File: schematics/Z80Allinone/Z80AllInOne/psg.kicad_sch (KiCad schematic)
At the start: 19 parts, among them J5 Conn_01x03_Male, J7 KEYBOARD_HEADER, U20 74LS02, U21 AY-3-8910, U22 LM386

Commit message: Latest modifications of All-in-one PCB
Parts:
- removed J5: Conn_01x03_Male, Connector_PinHeader_2.54mm:PinHeader_1x03_P2.54mm_Vertical, symbol Connector:Conn_01x03_Male
- removed JP4: PREAMP_MONO, Connector_PinHeader_2.54mm:PinHeader_2x03_P2.54mm_Vertical, symbol Connector_Generic:Conn_02x03_Odd_Even
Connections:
- net at R12.2, R13.2: now also U21.3 (ACH_B), U21.38 (ACH_C), U21.4 (ACH_A)
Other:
- moved on the sheet: C30, C31, C32, C33, C42, C43, R12, R13, R14, R15, SPEAKER1, U22

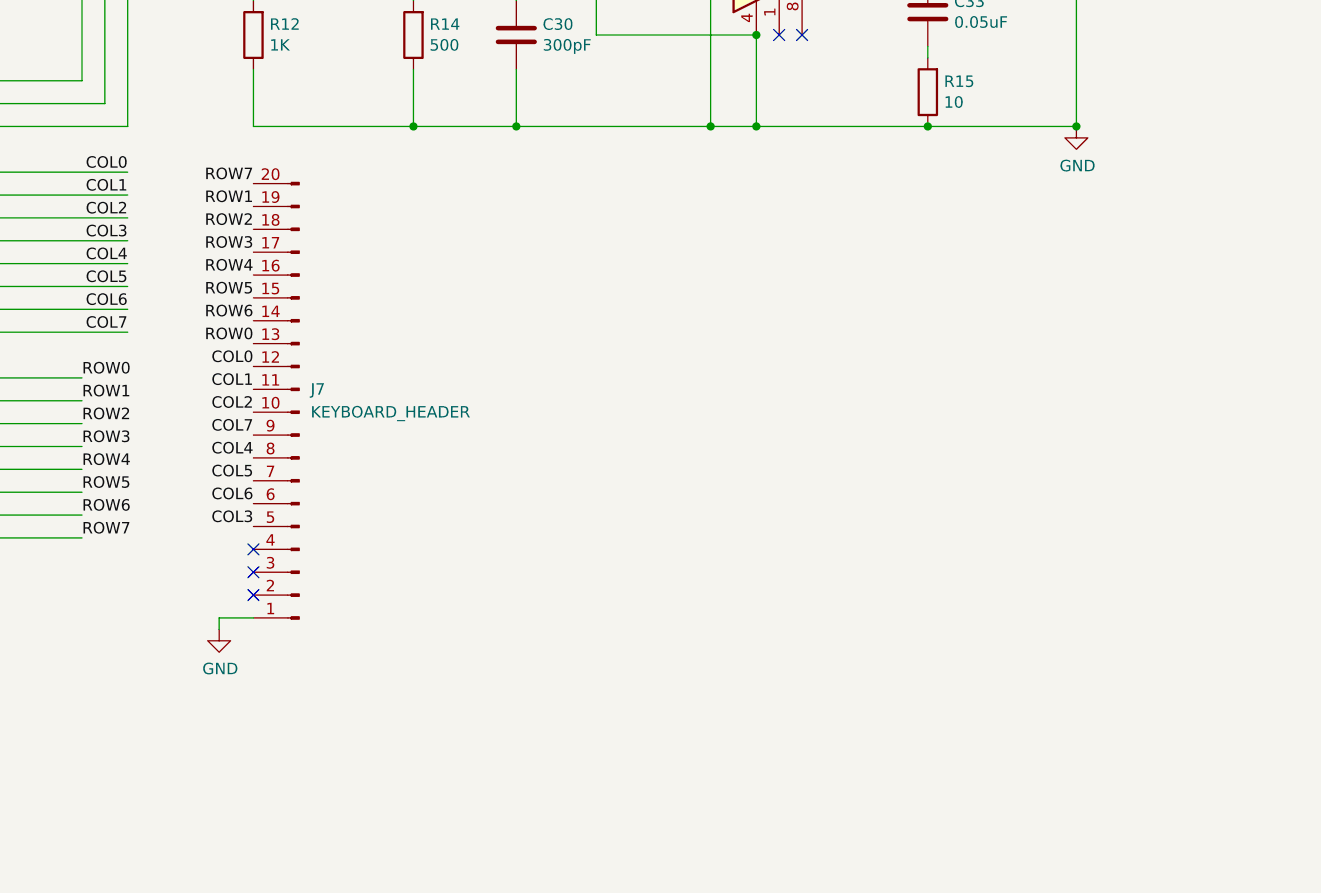
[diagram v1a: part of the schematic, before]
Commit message: Latest changes and replace CTC for 8253 PIT
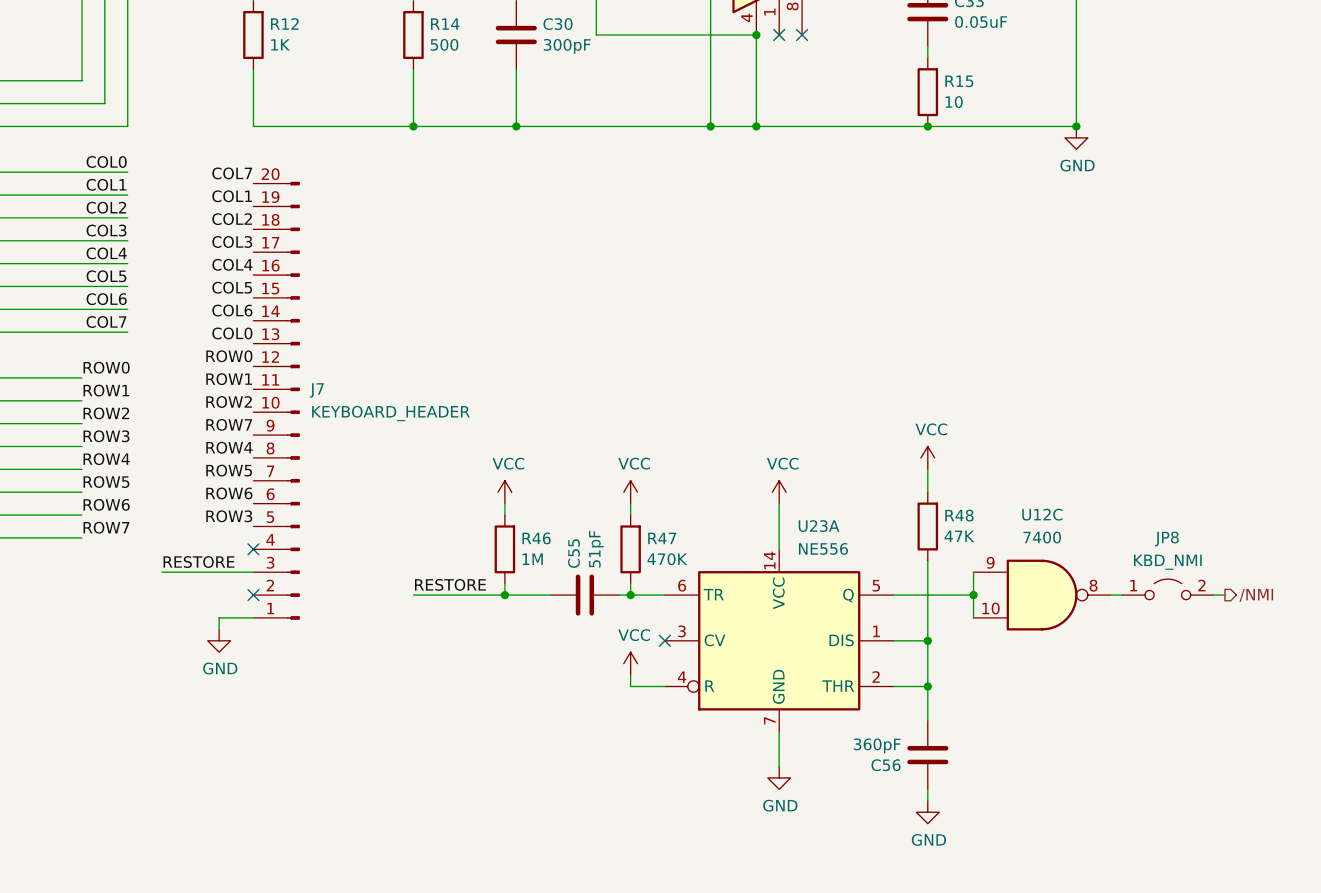
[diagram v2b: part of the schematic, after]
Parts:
- added C55: 51pF, Capacitor_THT:C_Disc_D5.0mm_W2.5mm_P5.00mm, symbol Device:C
- added C56: 360pF, Capacitor_THT:C_Disc_D5.0mm_W2.5mm_P5.00mm, symbol Device:C
- added JP8: KBD_NMI, Connector_PinHeader_2.54mm:PinHeader_1x02_P2.54mm_Vertical, symbol Jumper:Jumper_2_Open
- added R46: 1M, Resistor_THT:R_Axial_DIN0207_L6.3mm_D2.5mm_P10.16mm_Horizontal, symbol Device:R
- added R47: 470K, Resistor_THT:R_Axial_DIN0207_L6.3mm_D2.5mm_P10.16mm_Horizontal, symbol Device:R
- added R48: 47K, Resistor_THT:R_Axial_DIN0207_L6.3mm_D2.5mm_P10.16mm_Horizontal, symbol Device:R
- added U12: 7400, Package_DIP:DIP-14_W7.62mm_LongPads, symbol 74xx:7400
- added U23: NE556, Package_DIP:DIP-14_W7.62mm_LongPads, symbol Timer:NE556
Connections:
- net COL0: now also J7.13 (Pin_13); no longer J7.12 (Pin_12)
- net COL1: now also J7.19 (Pin_19); no longer J7.11 (Pin_11)
- net COL2: now also J7.18 (Pin_18); no longer J7.10 (Pin_10)
- net COL3: now also J7.17 (Pin_17); no longer J7.5 (Pin_5)
- net COL4: now also J7.16 (Pin_16); no longer J7.8 (Pin_8)
- net COL5: now also J7.15 (Pin_15); no longer J7.7 (Pin_7)
- net COL6: now also J7.14 (Pin_14); no longer J7.6 (Pin_6)
- net COL7: now also J7.20 (Pin_20); no longer J7.9 (Pin_9)
- net GND: now also C56.1, U23.7 (GND)
- net ROW0: now also J7.12 (Pin_12); no longer J7.13 (Pin_13)
- net ROW1: now also J7.11 (Pin_11); no longer J7.19 (Pin_19)
- net ROW2: now also J7.10 (Pin_10); no longer J7.18 (Pin_18)
- net ROW3: now also J7.5 (Pin_5); no longer J7.17 (Pin_17)
- net ROW4: now also J7.8 (Pin_8); no longer J7.16 (Pin_16)
- net ROW5: now also J7.7 (Pin_7); no longer J7.15 (Pin_15)
- net ROW6: now also J7.6 (Pin_6); no longer J7.14 (Pin_14)
- net ROW7: now also J7.9 (Pin_9); no longer J7.20 (Pin_20)
- net VCC: now also R46.2, R47.2, R48.2, U23.14 (VCC), U23.4 (R)
- net RESTORE: now reaches J7.3 (Pin_3)
- net RESTORE: now also C55.1, R46.1
- new net: C55.2, R47.1, U23.6 (TR)
- new net: JP8.1 (A), U12.8
- new net: C56.2, R48.1, U23.1 (DIS), U23.2 (THR)
- new net: U12.10, U12.9, U23.5 (Q)
- new net /NMI: JP8.2 (B)

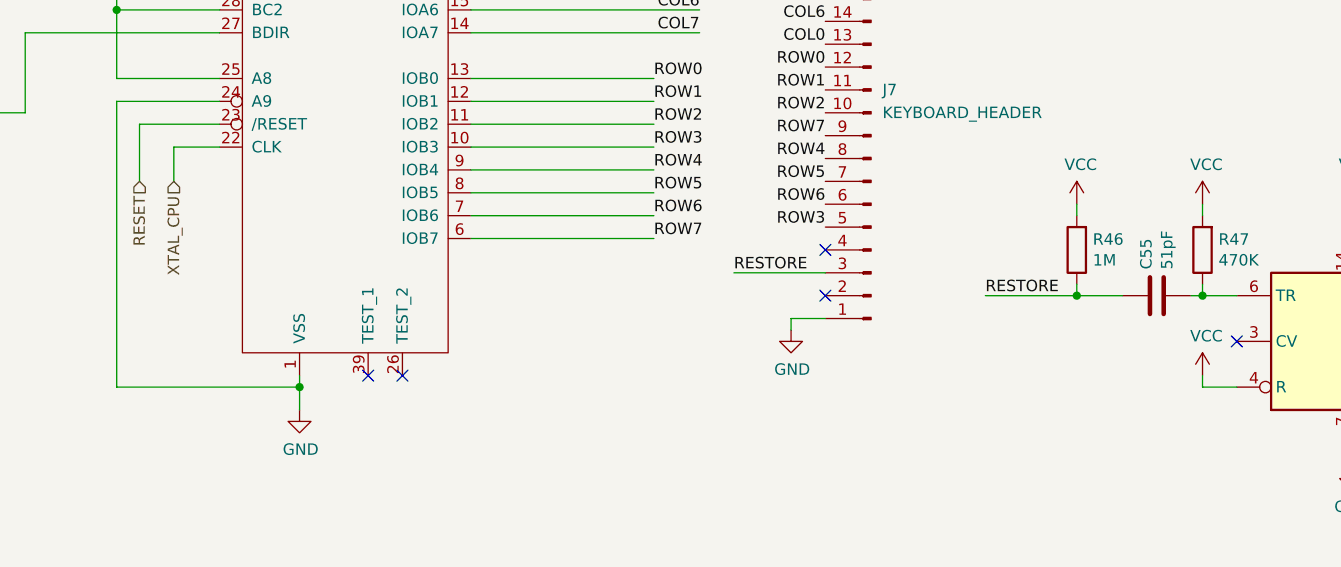
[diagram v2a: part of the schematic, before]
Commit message: Created new macro for LOADCNT PIT counter reset and removed old CTC routines that not used.
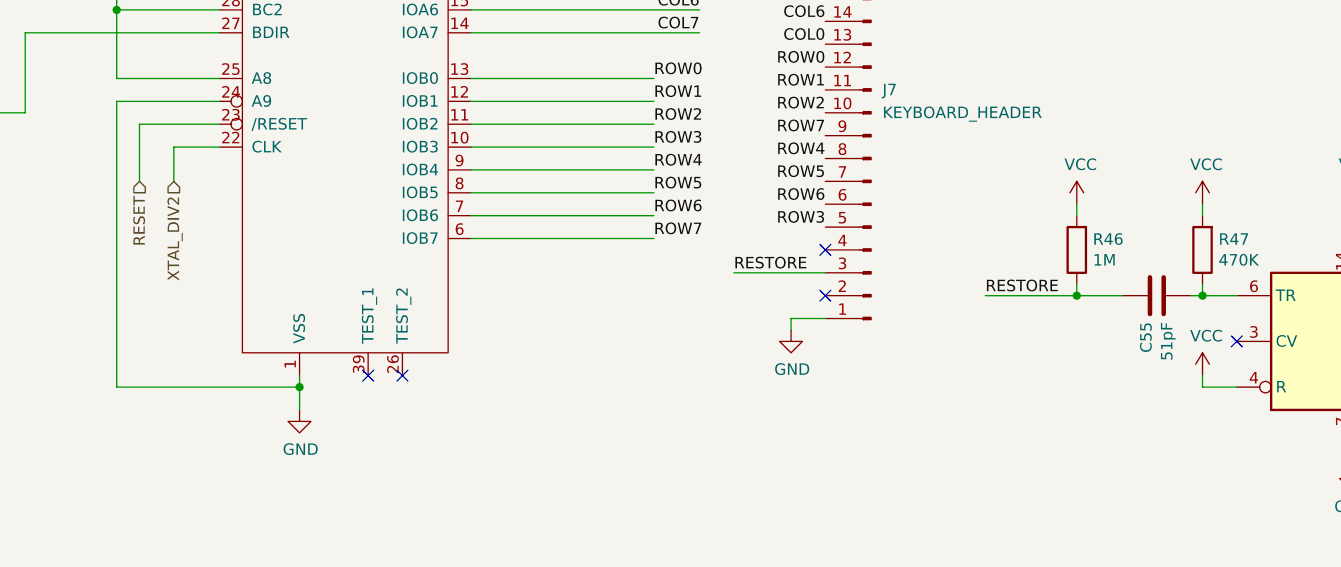
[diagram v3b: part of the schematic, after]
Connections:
- net XTAL_CPU renamed XTAL_DIV2
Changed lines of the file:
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@@
     (effects (font (size 1.27 1.27)) (justify right))
   )
-  (hierarchical_label "XTAL_CPU" (shape input) (at 92.71 121.92 270)
+  (hierarchical_label "XTAL_DIV2" (shape input) (at 92.71 121.92 270)
     (effects (font (size 1.27 1.27)) (justify right))
   )
@@
     (pin "2")
   )
-  (symbol (lib_id "Device:C") (at 201.93 134.62 90) (unit 1)
-    (in_bom yes) (on_board yes)
-    (property "Reference" "C55" (id 0) (at 200.7616 131.699 0)
-      (effects (font (size 1.27 1.27)) (justify left))
-    )
-    (property "Value" "51pF" (id 1) (at 203.073 131.699 0)
-      (effects (font (size 1.27 1.27)) (justify left))
-    )
-    (property "Footprint" "Capacitor_THT:C_Disc_D5.0mm_W2.5mm_P5.00mm" (id 2) (at 205.74 133.6548 0)
-      (effects (font (size 1.27 1.27)) hide)
-    )
+  (symbol (lib_id "Device:C") (at 201.93 134.62 90) (mirror x) (unit 1)
+    (in_bom yes) (on_board yes)
+    (property "Reference" "C55" (id 0) (at 200.7616 137.541 0)
+      (effects (font (size 1.27 1.27)) (justify left))
+    )
+    (property "Value" "51pF" (id 1) (at 203.073 137.541 0)
+      (effects (font (size 1.27 1.27)) (justify left))
+    )
+    (property "Footprint" "Capacitor_THT:C_Disc_D5.0mm_W2.5mm_P5.00mm" (id 2) (at 205.74 135.5852 0)
+      (effects (font (size 1.27 1.27)) hide)
+    )
